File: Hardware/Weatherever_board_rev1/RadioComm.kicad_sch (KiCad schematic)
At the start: 31 parts, among them J401 RF2-03-T-00-50-G, U401 CC110LRGPR, Y401 3225-27M-SR

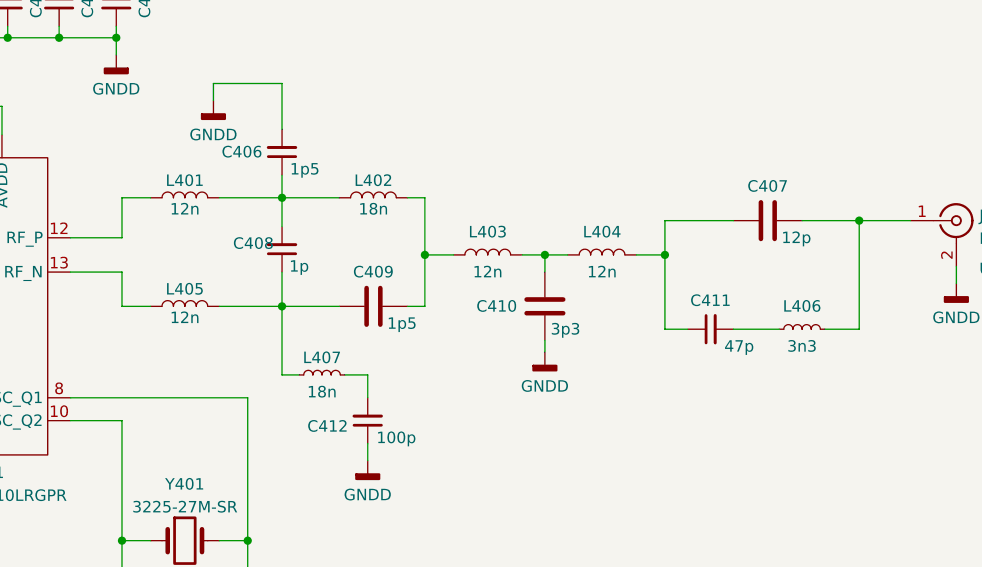
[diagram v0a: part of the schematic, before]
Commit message: New hw element and CommHandler tests
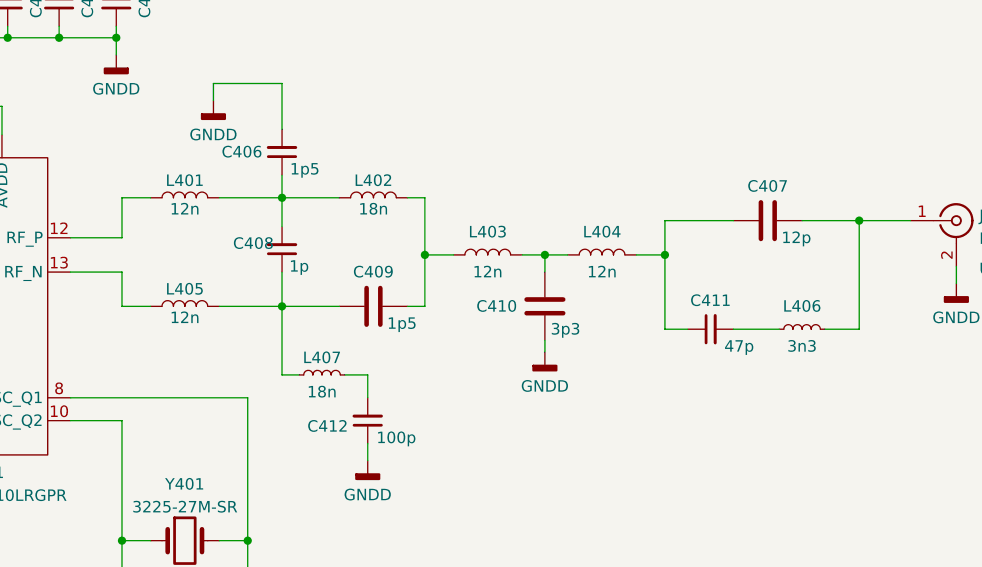
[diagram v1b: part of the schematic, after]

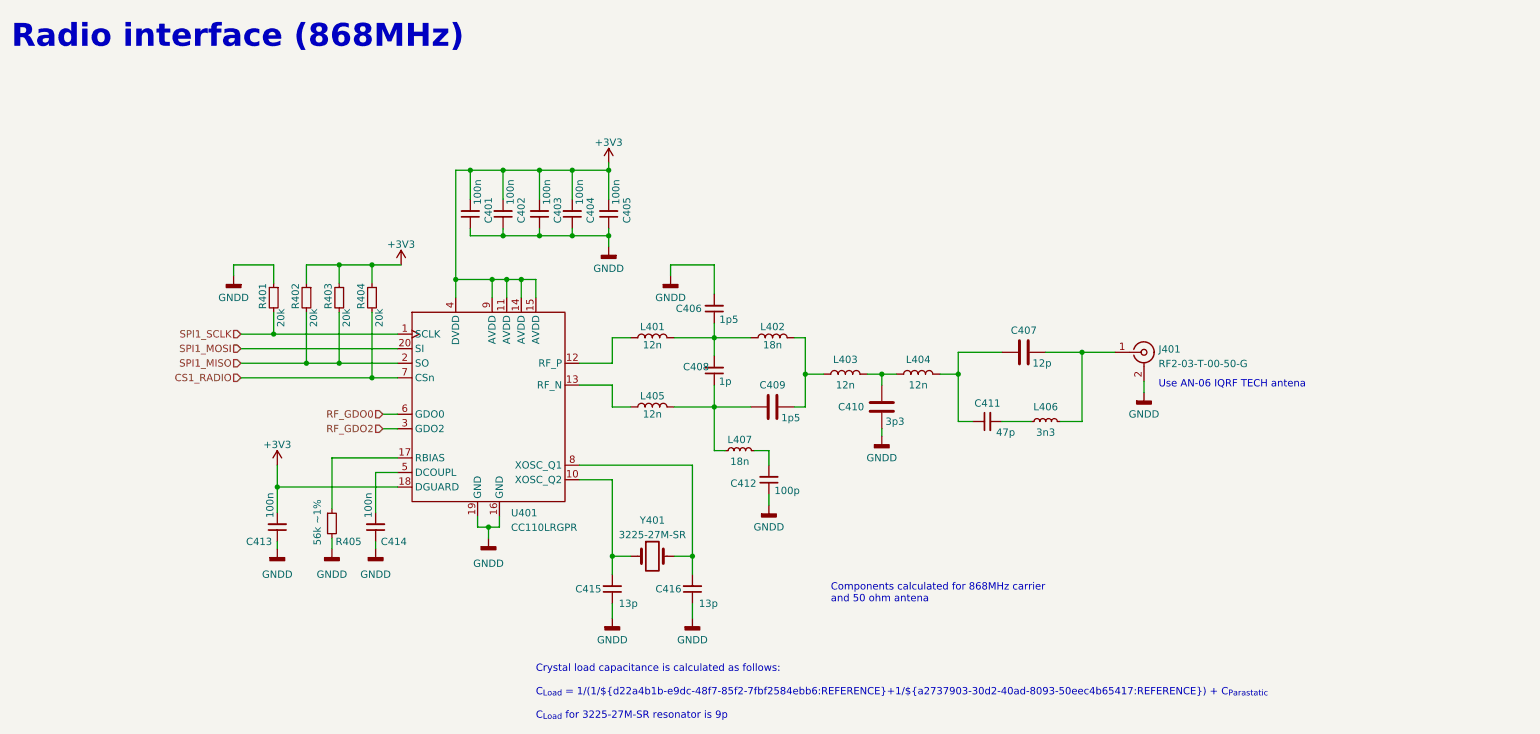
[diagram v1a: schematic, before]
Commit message: Funished schematics and GPIO drv interface
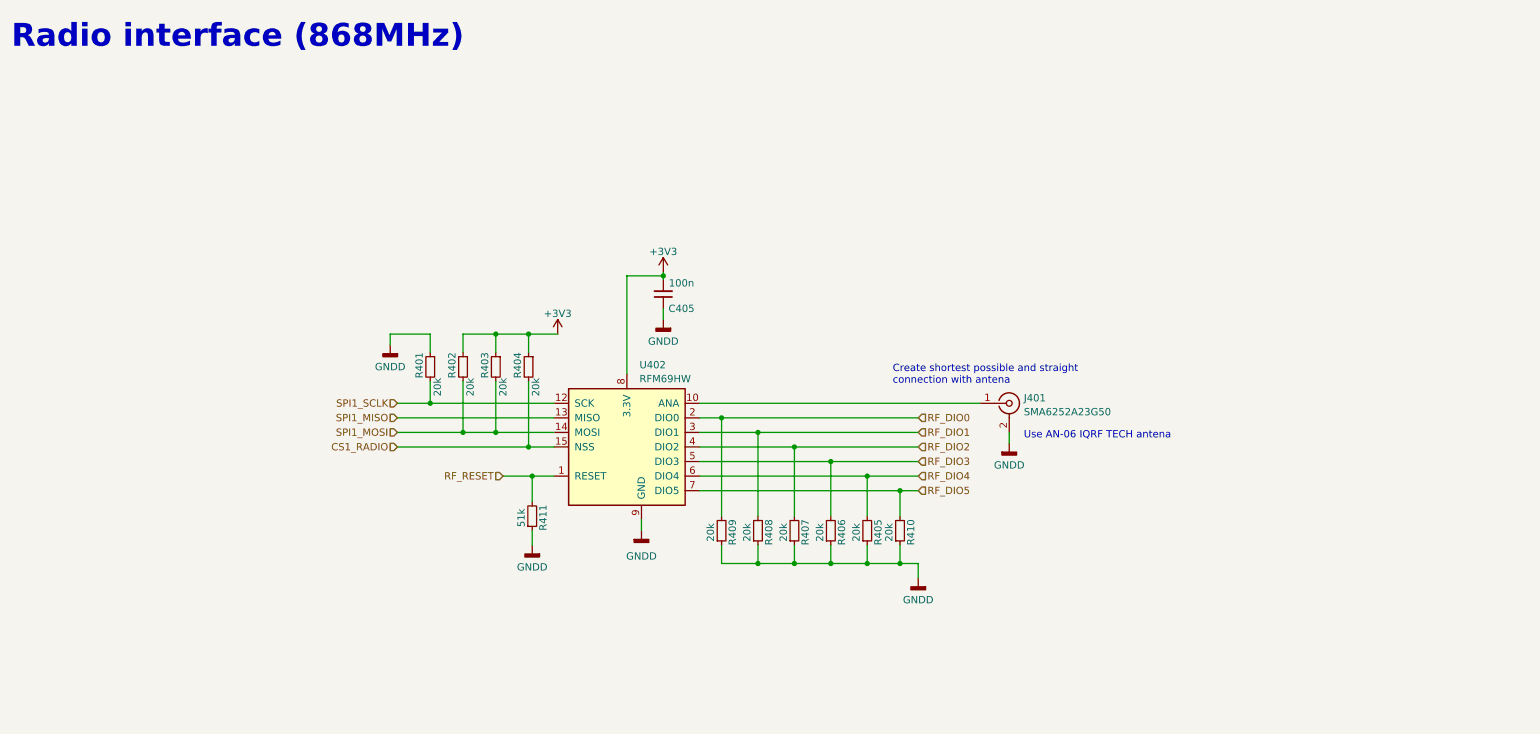
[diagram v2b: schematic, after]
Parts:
- removed C401, C402, C403, C404, C413, C414: 100n, Capacitor_SMD:C_0805_2012Metric_Pad1.18x1.45mm_HandSolder, symbol Device:C_Small
- removed C406: 1p5, Capacitor_SMD:C_0805_2012Metric_Pad1.18x1.45mm_HandSolder, symbol Device:C_Small
- removed C407: 12p, symbol Device:C
- removed C408: 1p, Capacitor_SMD:C_0805_2012Metric_Pad1.18x1.45mm_HandSolder, symbol Device:C_Small
- removed C409: 1p5, symbol Device:C
- removed C410: 3p3, symbol Device:C
- removed C411: 47p, symbol Device:C_Small
- removed C412: 100p, Capacitor_SMD:C_0805_2012Metric_Pad1.18x1.45mm_HandSolder, symbol Device:C_Small
- removed C415, C416: 13p, symbol Device:C_Small
- removed L401, L403, L404, L405: 12n, symbol Device:L
- removed L402: 18n, symbol Device:L
- removed L406: 3n3, symbol Device:L_Small
- removed L407: 18n, symbol Device:L_Small
- removed U401: CC110LRGPR, Package_DFN_QFN:QFN-20-1EP_4x4mm_P0.5mm_EP2.5x2.5mm_ThermalVias, symbol CustomSymbols:CC110LRGPR
- removed Y401: 3225-27M-SR, symbol Device:Crystal
- added R406, R407, R408, R409, R410: 20k, Resistor_SMD:R_0805_2012Metric_Pad1.20x1.40mm_HandSolder, symbol Device:R_Small
- added R411: 51k, Resistor_SMD:R_0805_2012Metric_Pad1.20x1.40mm_HandSolder, symbol Device:R_Small
- added U402: RFM69HW, RF_Module:HOPERF_RFM69HW, symbol RF_Module:RFM69HW
- J401: value RF2-03-T-00-50-G -> SMA6252A23G50; footprint (none) -> Connector_Coaxial:SMA_Amphenol_901-143_Horizontal
- R405: value 56k ~1% -> 20k; footprint (none) -> Resistor_SMD:R_0805_2012Metric_Pad1.20x1.40mm_HandSolder
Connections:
- net +3V3: now also U402.8 (3.3V)
- net CS1_RADIO: now also U402.15 (NSS)
- net GNDD: now also R405.1, R406.1, R407.1, R408.1, R409.1, R410.1, R411.1, U402.11 (GND), U402.9 (GND); no longer R405.2
- net SPI1_MISO: now also U402.13 (MISO); no longer R402.2, R403.2
- net SPI1_MOSI: now also R402.2, R403.2, U402.14 (MOSI)
- net SPI1_SCLK: now also U402.12 (SCK)
- net at J401.1 (In): now also U402.10 (ANA)
- new net RF_DIO0: R409.2, U402.2 (DIO0)
- new net RF_DIO1: R408.2, U402.3 (DIO1)
- new net RF_DIO2: R407.2, U402.4 (DIO2)
- new net RF_DIO3: R406.2, U402.5 (DIO3)
- new net RF_DIO4: R405.2, U402.6 (DIO4)
- new net RF_DIO5: R410.2, U402.7 (DIO5)
- new net RF_RESET: R411.2, U402.1 (RESET)
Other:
- note added: "Create shortest possible and straight connection with antena"
- note removed: "Components calculated for 868MHz carrier and 50 ohm antena"
- note removed: "Crystal load capacitance is calculated as follows: C_{Load} = 1/(1/${d22a4b1b-e9dc-48f7-85f2-7fbf2584ebb6:REFERENCE}+1/${a2737903-30d2-40ad-8093-50eec4b65417:REFERENCE}) + C_{Parastatic} C_{Load} for 3225-27M-SR resonator is 9p"
- moved on the sheet: C405, J401, R401, R402, R403, R404

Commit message: Layout impl start
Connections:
- net ANT_OUT: now reaches J401.1 (In), U402.10 (ANA)
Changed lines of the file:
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@@
   (junction (at 161.29 100.33) (diameter 0) (color 0 0 0 0)
   )
+  (junction (at 166.37 92.71) (diameter 0) (color 0 0 0 0)
+  )
   (junction (at 167.64 102.87) (diameter 0) (color 0 0 0 0)
   )
@@
     (stroke (width 0) (type default))
   )
+  (wire (pts (xy 166.37 90.805) (xy 166.37 92.71))
+    (stroke (width 0) (type default))
+  )
   (wire (pts (xy 154.94 97.79) (xy 182.88 97.79))
     (stroke (width 0) (type default))
@@
     (stroke (width 0) (type default))
   )
-  (wire (pts (xy 144.78 92.71) (xy 193.675 92.71))
+  (wire (pts (xy 144.78 92.71) (xy 166.37 92.71))
     (stroke (width 0) (type default))
   )
@@
   )
   (wire (pts (xy 167.64 102.87) (xy 167.64 112.395))
+    (stroke (width 0) (type default))
+  )
+  (wire (pts (xy 166.37 92.71) (xy 193.675 92.71))
     (stroke (width 0) (type default))
   )
@@
     (effects (font (size 1.27 1.27)) (justify left bottom))
   )
+  (label "ANT_OUT" (at 166.37 90.805 180) (fields_autoplaced)
+    (effects (font (size 1.27 1.27)) (justify right bottom))
+  )
   (hierarchical_label "RF_DIO2" (shape input) (at 182.88 100.33 0) (fields_autoplaced)
